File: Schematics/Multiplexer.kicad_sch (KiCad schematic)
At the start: 88 parts, among them J16 Conn_01x04, J17 Conn_01x03, J18 Conn_01x03, J19 Conn_01x03, J33 Conn_01x04, J34 Conn_01x04, J35 Conn_01x04, J36 Conn_01x04, J37 Conn_01x04, J38 Conn_01x04, J39 Conn_01x04, J40 Conn_01x02, Q7 BSS138, Q8 BSS138, U41 TL072, U43 LM1117-5, U44 PCF8575, U45 LM1117-3.3, U47 DG212C, U48 DG212C, U49 DG212C, U50 DG212C

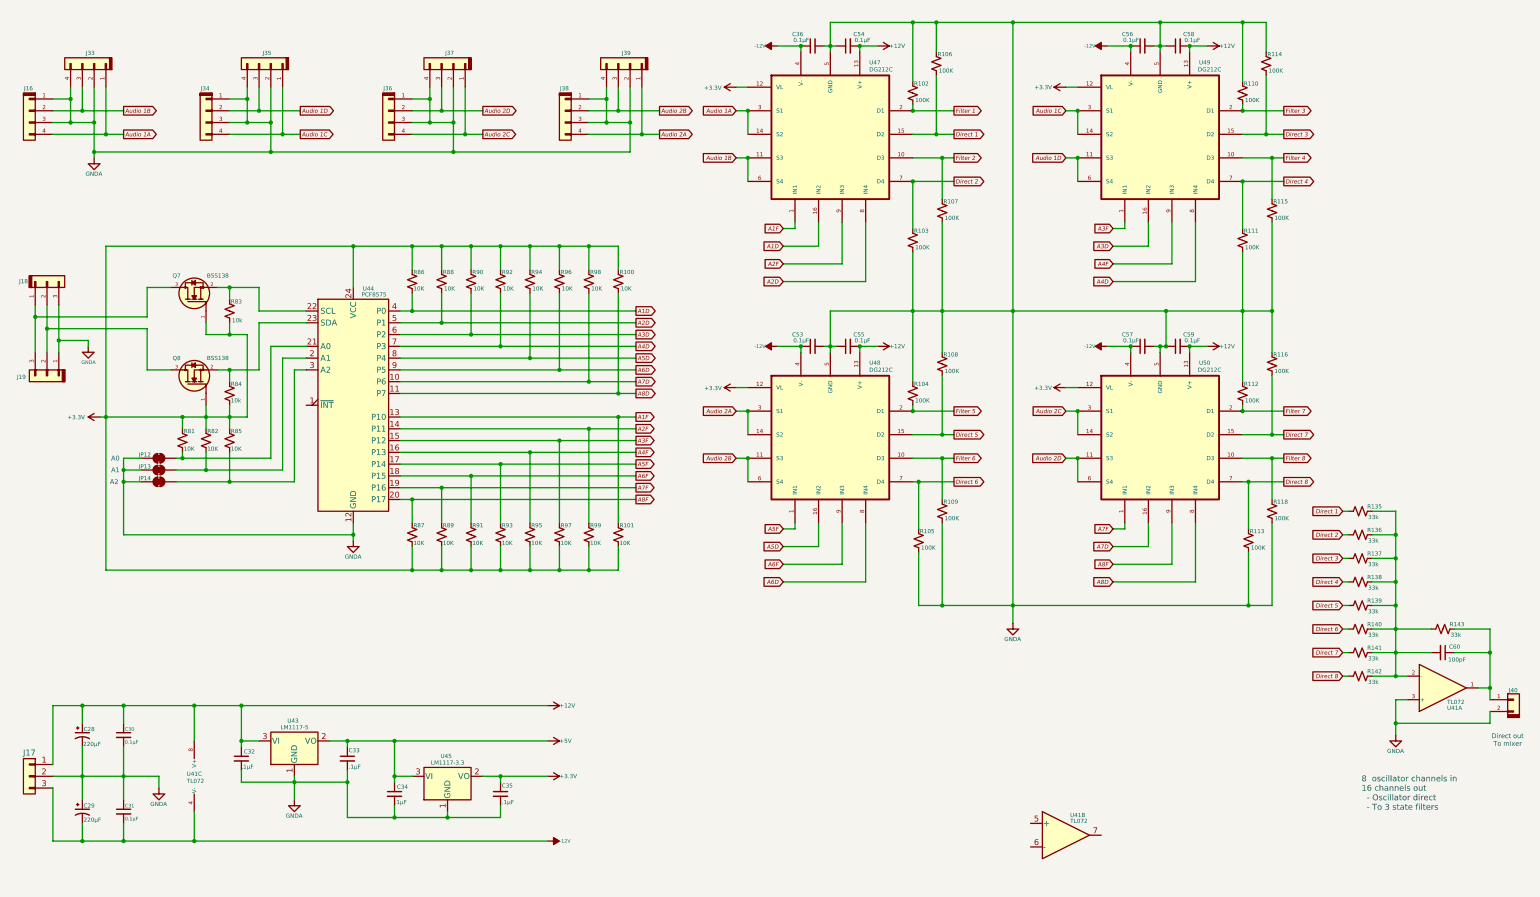
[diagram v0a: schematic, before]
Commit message: All Oscillators have thier own D/A converters and both LFOs are working.  Callibration functions.
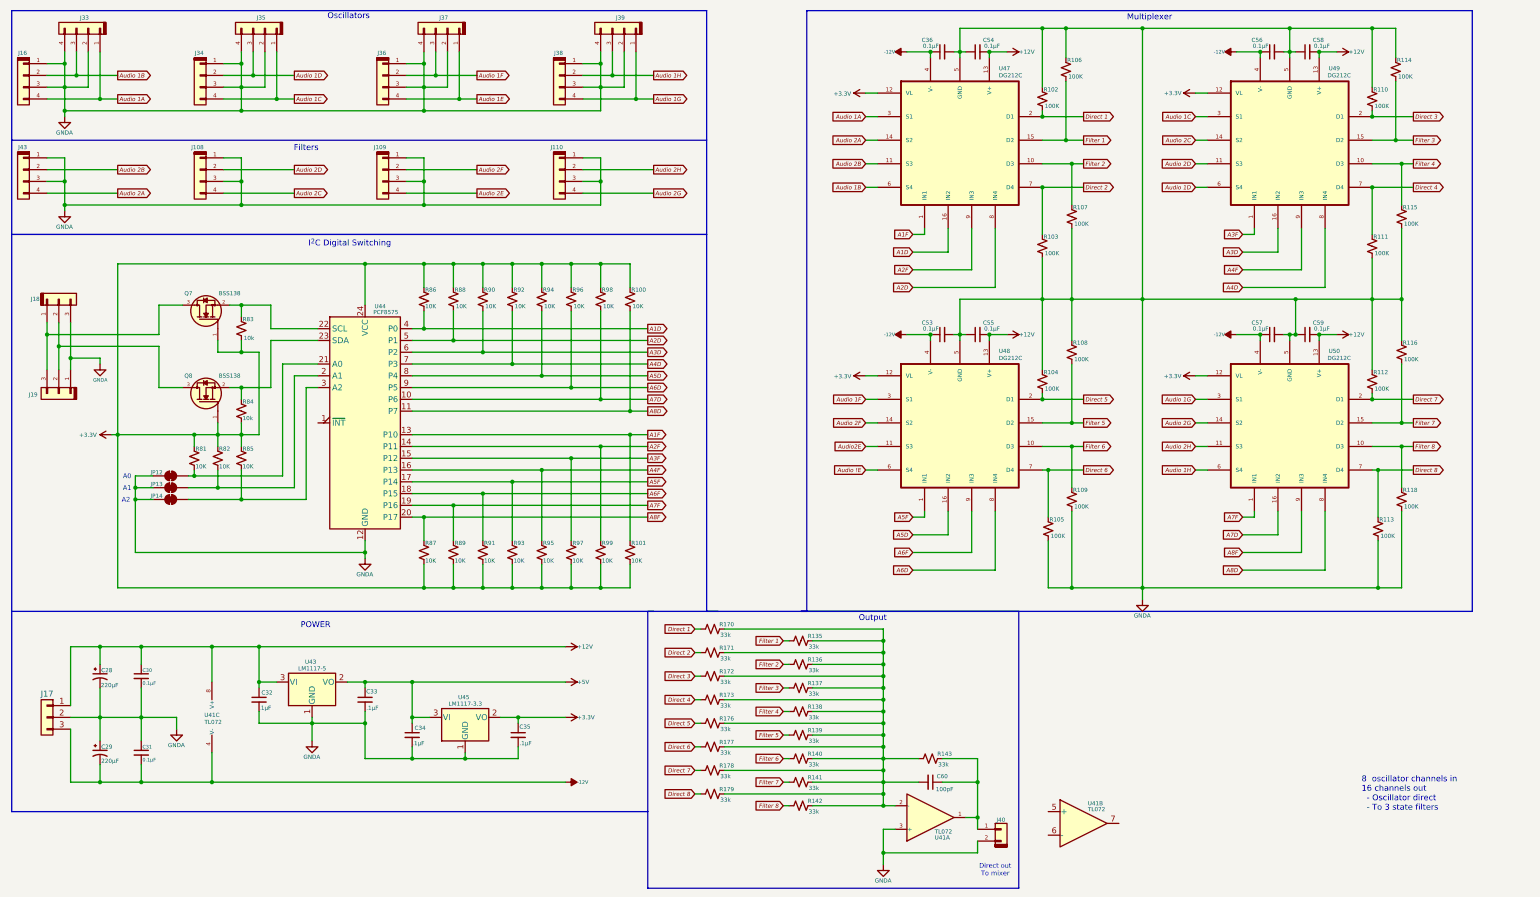
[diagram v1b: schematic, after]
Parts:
- added J108, J109, J110, J43: Conn_01x04, symbol My Connectors:Conn_01x04
- added R170, R171, R172, R173, R176, R177, R178, R179: 33k, symbol Device:R_Small_US
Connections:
- net Audio 1A: no longer U47.14 (S2)
- net Audio 1B: no longer U47.11 (S3)
- net Audio 1C: no longer U49.14 (S2)
- net Audio 1D: no longer U49.11 (S3)
- net Audio 2A: now also U47.14 (S2), J43.4 (Pin_4); no longer J38.4 (Pin_4), J39.1 (Pin_1), U48.14 (S2), U48.3 (S1)
- net Audio 2B: now also U47.11 (S3), J43.2 (Pin_2); no longer J38.2 (Pin_2), J39.3 (Pin_3), U48.11 (S3), U48.6 (S4)
- net Audio 2C: now also U49.14 (S2), J108.4 (Pin_4); no longer J36.4 (Pin_4), J37.1 (Pin_1), U50.14 (S2), U50.3 (S1)
- net Audio 2D: now also U49.11 (S3), J108.2 (Pin_2); no longer J36.2 (Pin_2), J37.3 (Pin_3), U50.11 (S3), U50.6 (S4)
- net Direct 1: now also R102.2, U47.2 (D1), R170.1; no longer R106.2, R135.1, U47.15 (D2)
- net Direct 2: now also R171.1; no longer R136.1
- net Direct 3: now also R110.2, U49.2 (D1), R172.1; no longer R114.2, R137.1, U49.15 (D2)
- net Direct 4: now also R173.1; no longer R138.1
- net Direct 5: now also R104.2, U48.2 (D1), R176.1; no longer R108.2, R139.1, U48.15 (D2)
- net Direct 6: now also R177.1; no longer R140.1
- net Direct 7: now also R112.2, U50.2 (D1), R178.1; no longer R116.2, R141.1, U50.15 (D2)
- net Direct 8: now also R179.1; no longer R142.1
- net Filter 1: now also R106.2, R135.1, U47.15 (D2); no longer R102.2, U47.2 (D1)
- net Filter 2: now also R136.1
- net Filter 3: now also R114.2, R137.1, U49.15 (D2); no longer R110.2, U49.2 (D1)
- net Filter 4: now also R138.1
- net Filter 5: now also R108.2, R139.1, U48.15 (D2); no longer R104.2, U48.2 (D1)
- net Filter 6: now also R140.1
- net Filter 7: now also R116.2, R141.1, U50.15 (D2); no longer R112.2, U50.2 (D1)
- net Filter 8: now also R142.1
- net GNDA: now also J108.1 (Pin_1), J108.3 (Pin_3), J109.1 (Pin_1), J109.3 (Pin_3), J110.1 (Pin_1), J110.3 (Pin_3), J43.1 (Pin_1), J43.3 (Pin_3)
- net at C60.2, R135.2, R136.2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: now also R170.2, R171.2, R172.2, R173.2, R176.2, R177.2, R178.2, R179.2
- new net Audio !E: U48.6 (S4)
- new net Audio 1E: J36.4 (Pin_4), J37.1 (Pin_1)
- new net Audio 1F: J36.2 (Pin_2), J37.3 (Pin_3), U48.3 (S1)
- new net Audio 1G: J38.4 (Pin_4), J39.1 (Pin_1), U50.3 (S1)
- new net Audio 1H: J38.2 (Pin_2), J39.3 (Pin_3), U50.6 (S4)
- new net Audio 2E: J109.4 (Pin_4)
- new net Audio 2F: J109.2 (Pin_2), U48.14 (S2)
- new net Audio 2G: J110.4 (Pin_4), U50.14 (S2)
- new net Audio 2H: J110.2 (Pin_2), U50.11 (S3)
- new net Audio2E: U48.11 (S3)
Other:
- note added: "Filters"
- note added: "I^{2}C Digital Switching"
- note added: "Multiplexer"
- note added: "Oscillators"
- note added: "Output"
- note added: "POWER"
- moved on the sheet: C28, C29, C30, C31, C32, C33, C34, C35, C36, C53, C54, C55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

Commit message: Fixed bugs in voice selection on configuration.  Reorganized schematics to have different master drawings for power and audio paths.  Started work on dual 3-pole state variable filter with resonance.
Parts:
- renumbered C28 to C319, C29 to C320, C30 to C329, C31 to C330, C32 to C352, C33 to C370, C34 to C377, C35 to C388, C60 to C433, C36 to C434, C53 to C435, C54 to C439, C55 to C440, C56 to C459, C57 to C460, C58 to C461, C59 to C462, J16 to J204, J43 to J206, J17 to J218, J18 to J223, J19 to J224, J33 to J228, J34 to J233, J108 to J234, J35 to J237, J36 to J239, J109 to J240, J37 to J243, J38 to J245, J110 to J246, J39 to J247, J40 to J268, JP12 to JP34, JP13 to JP35, JP14 to JP36, Q7 to Q34, Q8 to Q35, R81 to R579, R82 to R587, R83 to R594, R84 to R595, R85 to R596, R86 to R629, R87 to R630, R88 to R635, R89 to R636, R90 to R643, R91 to R644, R92 to R654, R93 to R656, R94 to R669, R95 to R670, R96 to R680, R97 to R681, R98 to R688, R99 to R689, R100 to R700, R101 to R701, R170 to R714, R171 to R715, R172 to R716, R173 to R717, R176 to R718, R177 to R719, R178 to R720, R179 to R721, R135 to R724, R136 to R725, R137 to R726, R138 to R727, R139 to R728, R140 to R729, R141 to R730, R142 to R731, R143 to R735, R102 to R756, R103 to R757, R104 to R759, R105 to R760, R106 to R761, R107 to R766, R108 to R767, R109 to R768, R110 to R787, R111 to R788, R112 to R789, R113 to R790, R114 to R791, R115 to R792, R116 to R793, R118 to R794, U41 to U211, U43 to U220, U44 to U227, U45 to U241, U47 to U274, U48 to U275, U49 to U299, U50 to U300

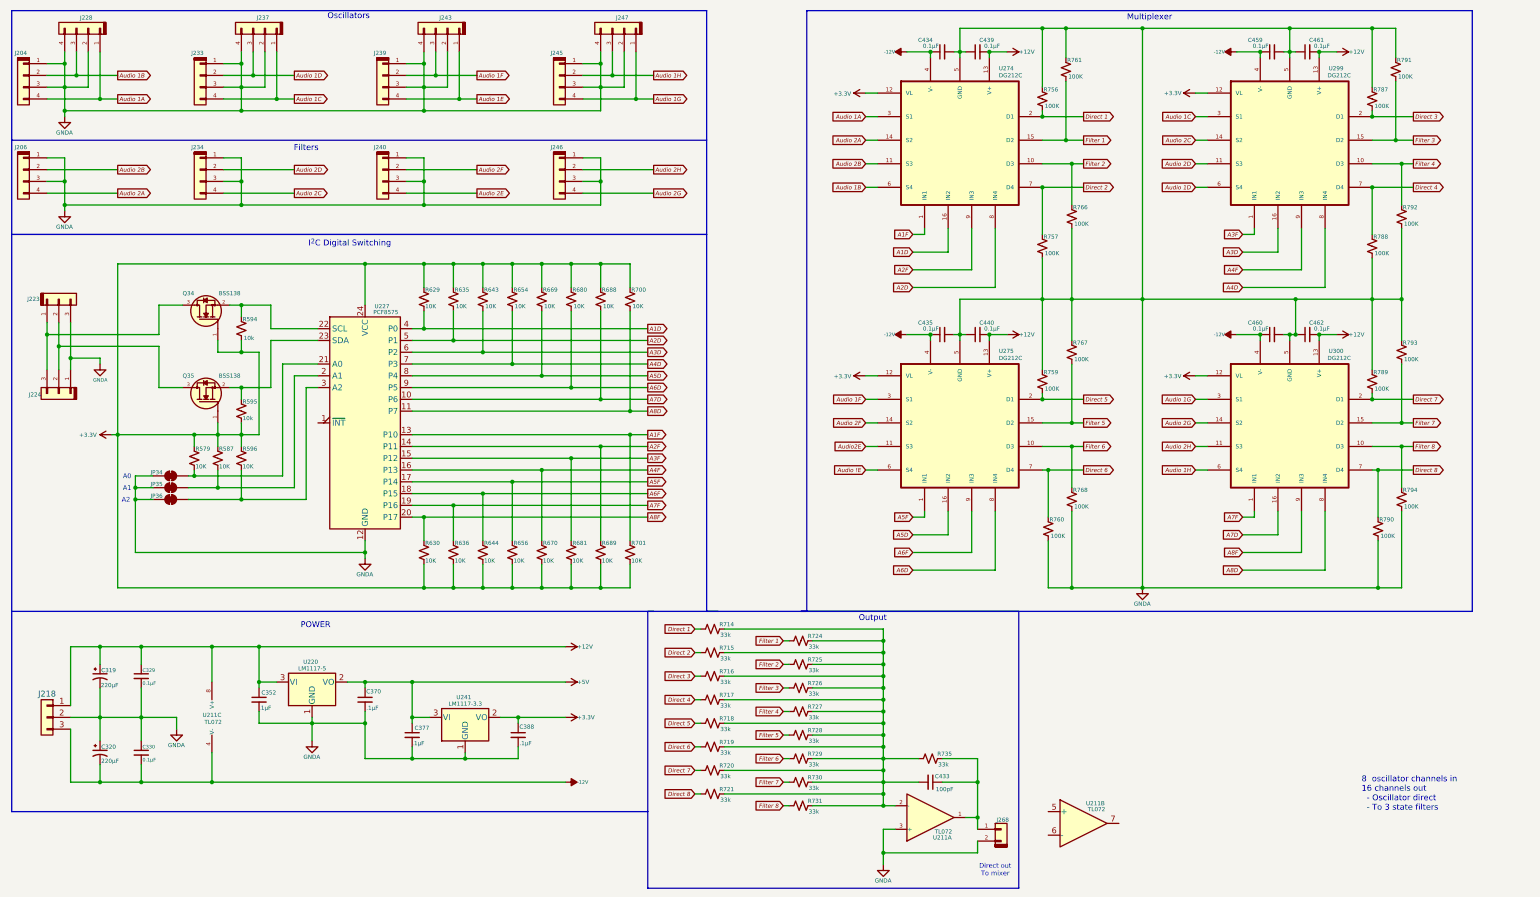
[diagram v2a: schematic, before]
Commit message: Fixed schematic errors.
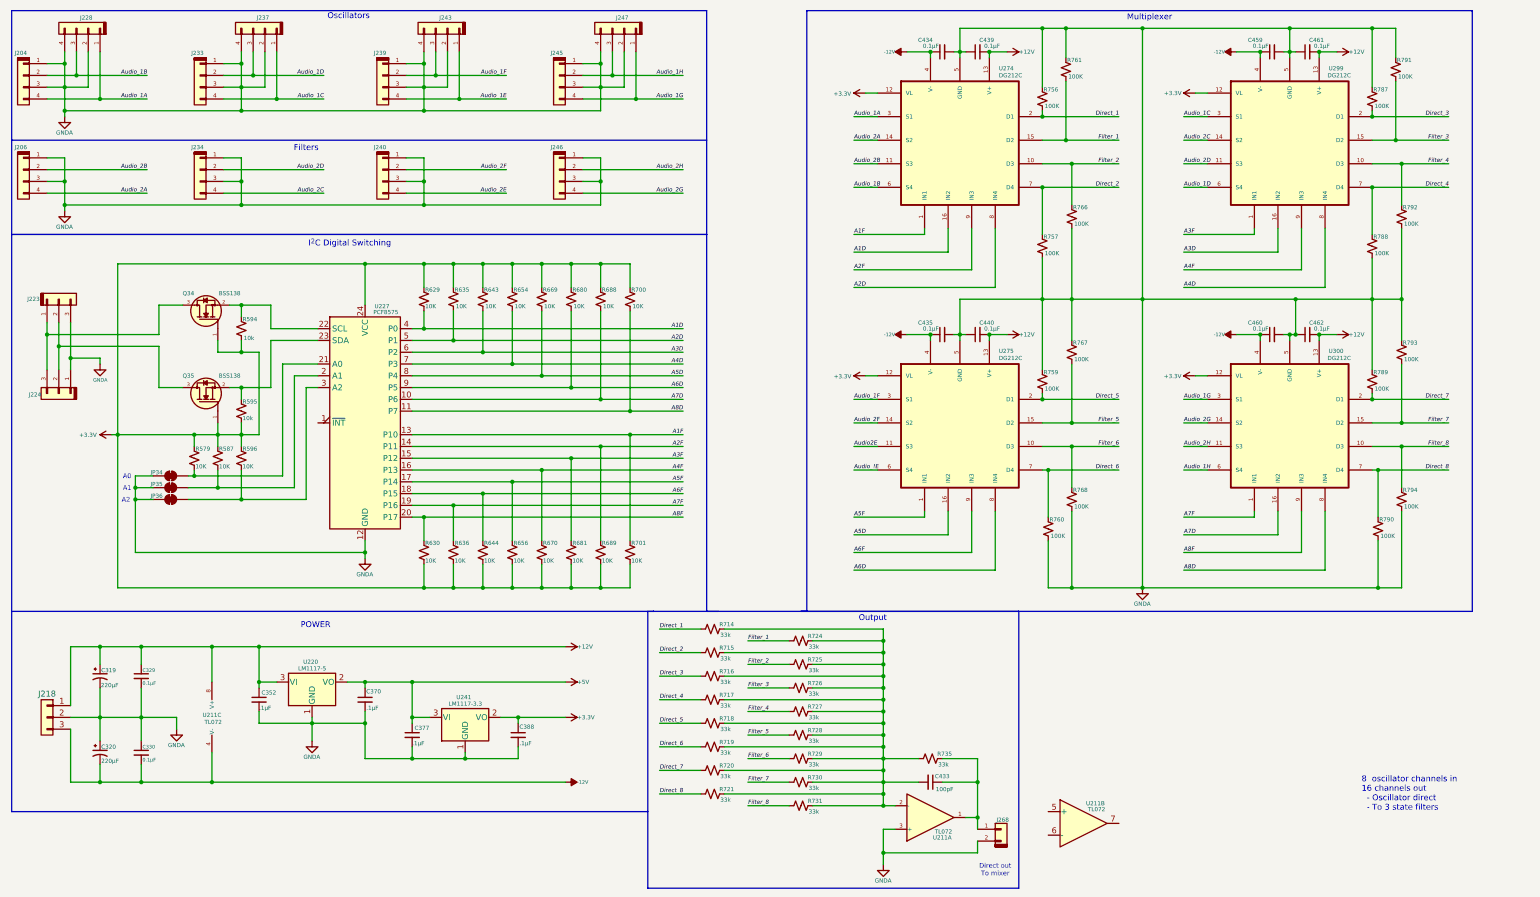
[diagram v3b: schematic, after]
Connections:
- net Audio !E renamed Audio_!E
- net Audio 1A renamed Audio_1A
- net Audio 1B renamed Audio_1B
- net Audio 1C renamed Audio_1C
- net Audio 1D renamed Audio_1D
- net Audio 1E renamed Audio_1E
- net Audio 1F renamed Audio_1F
- net Audio 1G renamed Audio_1G
- net Audio 1H renamed Audio_1H
- net Audio 2A renamed Audio_2A
- net Audio 2B renamed Audio_2B
- net Audio 2C renamed Audio_2C
- net Audio 2D renamed Audio_2D
- net Audio 2E renamed Audio_2E
- net Audio 2F renamed Audio_2F
- net Audio 2G renamed Audio_2G
- net Audio 2H renamed Audio_2H
- net Direct 1 renamed Direct_1
- net Direct 2 renamed Direct_2
- net Direct 3 renamed Direct_3
- net Direct 4 renamed Direct_4
- net Direct 5 renamed Direct_5
- net Direct 6 renamed Direct_6
- net Direct 7 renamed Direct_7
- net Direct 8 renamed Direct_8
- net Filter 1 renamed Filter_1
- net Filter 2 renamed Filter_2
- net Filter 3 renamed Filter_3
- net Filter 4 renamed Filter_4
- net Filter 5 renamed Filter_5
- net Filter 6 renamed Filter_6
- net Filter 7 renamed Filter_7
- net Filter 8 renamed Filter_8
